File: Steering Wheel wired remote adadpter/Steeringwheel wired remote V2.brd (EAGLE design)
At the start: 100 x 80 mm, 8 parts

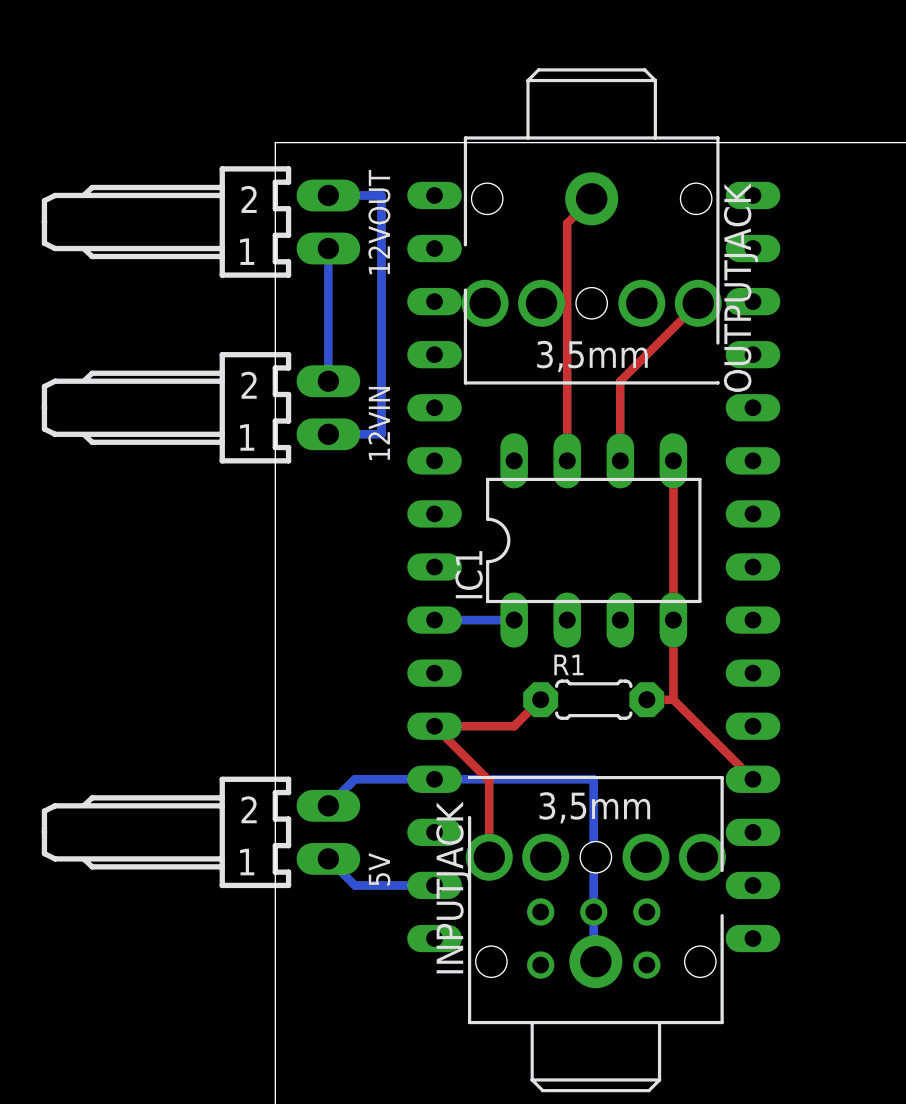
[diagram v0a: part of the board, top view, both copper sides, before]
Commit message: 3 pin jacks added
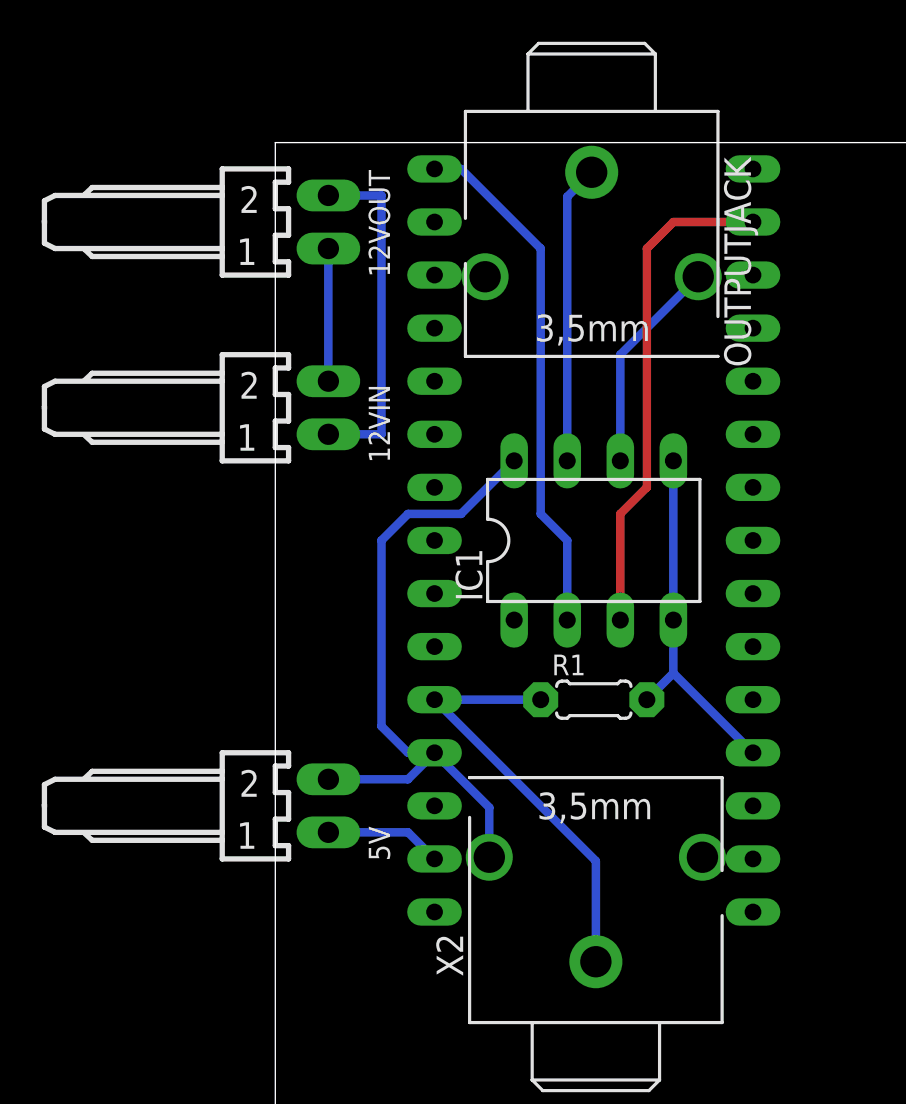
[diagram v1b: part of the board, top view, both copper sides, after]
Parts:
- removed INPUTJACK: STEREOJACK, adafruit:STX3100
- removed U$1: NANO, Arduino-clone:NANO
- added U$2: NANO, my_lib:NANO_NOISPC
- added X2: STEREOJACK_3PIN3PIN, my_lib:STX3000
- IC1: value (none) -> MCP4131
- OUTPUTJACK: value STEREOJACK -> STEREOJACK_3PIN3PIN; device adafruit:STX3100 -> my_lib:STX3000
- moved OUTPUTJACK 1.27 mm to (15.2, 78.7)
- moved 5V 1.27 mm to (2.54, 48.3)
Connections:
- removed net N$10: 5V.2, INPUTJACK.1, U$1.5V
- removed net N$11: IC1.1, U$1.A5
- new net N$2: IC1.2, U$2.D13
- net N$1: now also IC1.3, U$2.D11; no longer IC1.4, IC1.5, R1.2, U$1.GND1
- net N$3: now also IC1.4, IC1.5, R1.2, U$2.GND1; no longer IC1.2, U$1.D13
- net N$4: now also R1.1, U$2.A7, X2.1; no longer IC1.3, U$1.D11
- net N$6: now also 5V.2, IC1.8, U$2.5V, X2.2; no longer INPUTJACK.2, R1.1, U$1.A7
- net N$7: now also U$2.GND; no longer IC1.8, U$1.GND
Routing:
- net N$2: track 0.00 -> 25.0 mm
- net N$10: track 22.3 -> 0.00 mm, vias 1 -> 0
- net N$4: track 0.00 -> 20.8 mm
- net N$6: track 13.0 -> 31.6 mm
- net N$3: track 0.00 -> 17.3 mm
- net N$1: track 18.1 -> 23.9 mm
- net N$11: track 3.81 -> 0.00 mm
- net N$5: track 9.09 -> 10.4 mm
- net N$12: track 13.0 -> 14.3 mm

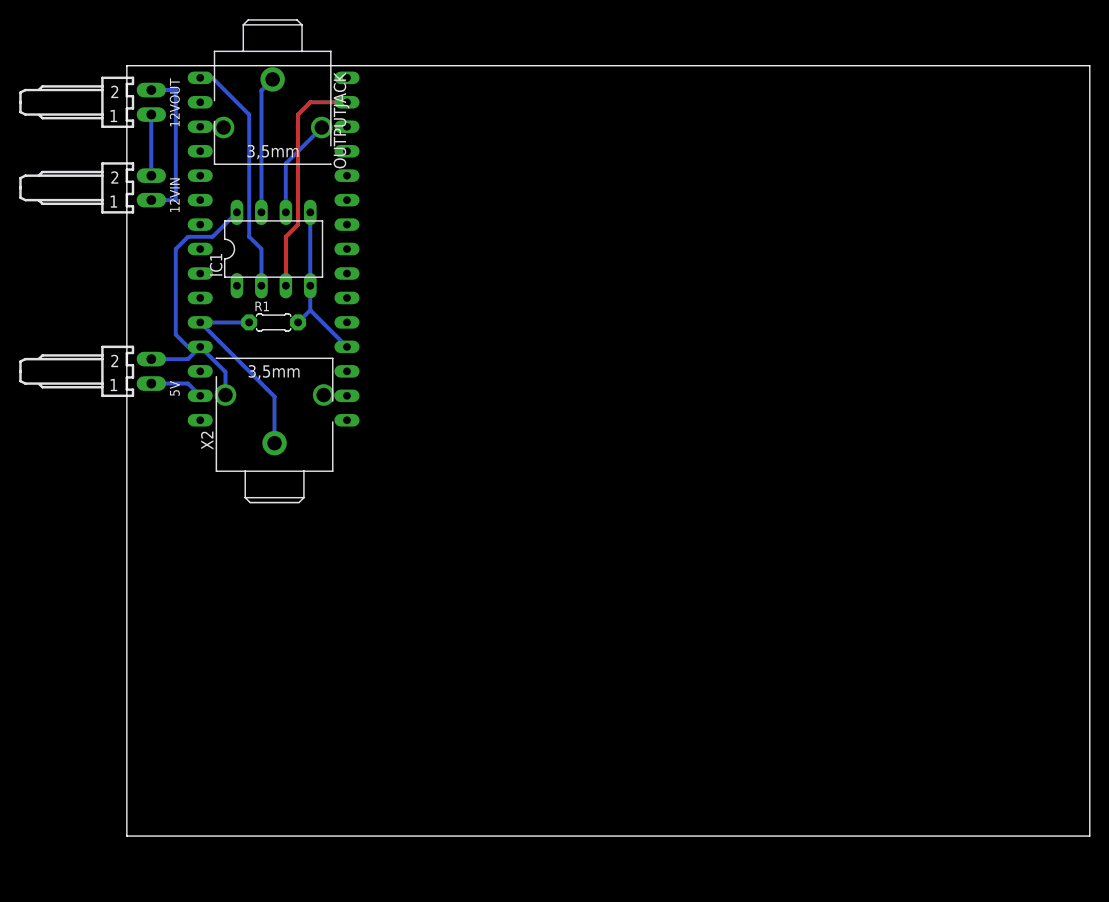
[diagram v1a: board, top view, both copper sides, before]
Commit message: GND copper poor and .024 traces
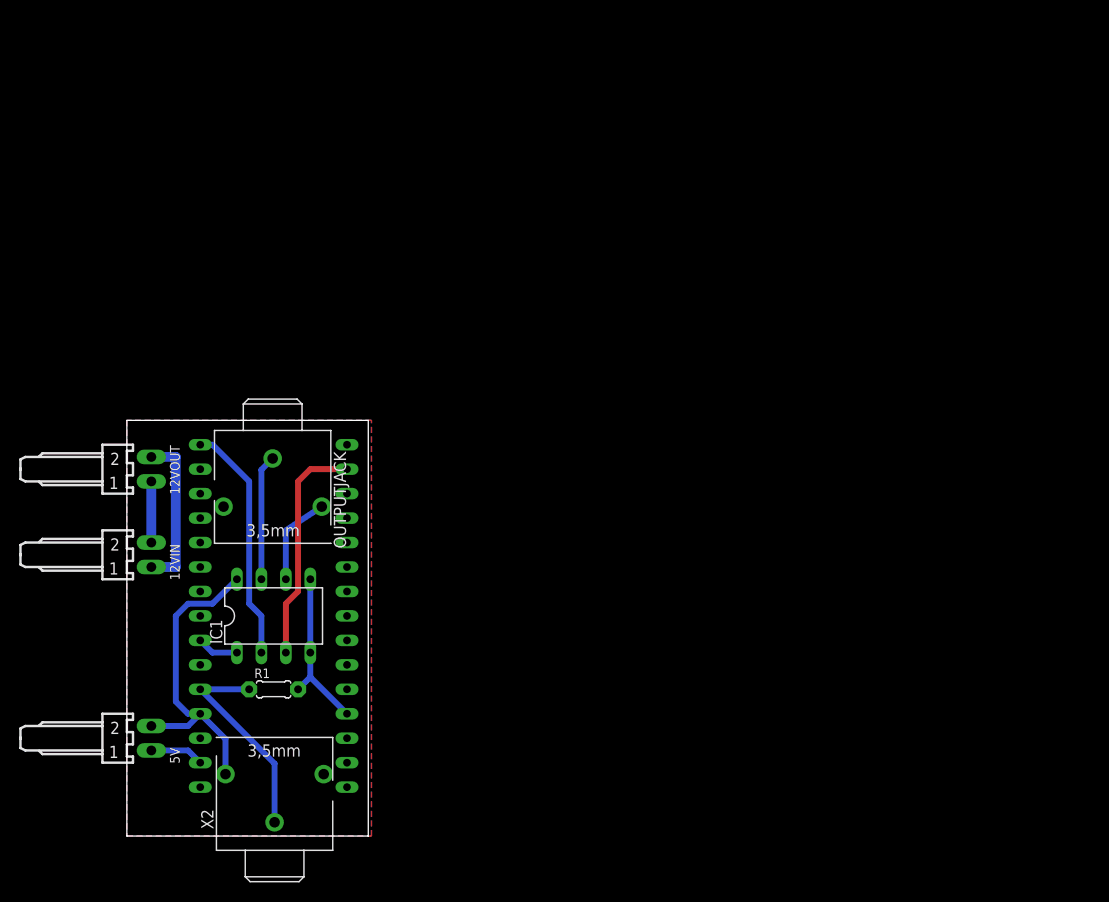
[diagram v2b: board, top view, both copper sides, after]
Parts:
- moved OUTPUTJACK 39.4 mm to (15.2, 39.4)
- moved X2 39.4 mm to (15.2, 1.27)
- moved 12VIN 38.1 mm to (2.54, 29.2)
- moved 12VOUT 38.1 mm to (2.54, 38.1)
- moved IC1 38.1 mm to (15.2, 22.9)
- moved R1 38.1 mm to (15.2, 15.2)
- moved U$2 38.1 mm to (17.8, 14.0)
- moved 5V 38.1 mm to (2.54, 10.2)
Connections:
- removed net N$3: IC1.4, IC1.5, R1.2, U$2.GND1
- removed net N$7: 5V.1, U$2.GND
- new net GND: 5V.1, IC1.4, IC1.5, R1.2, U$2.GND, U$2.GND1
- new net N$10: IC1.1, U$2.A5
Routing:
- net GND: track 0.00 -> 23.0 mm
- net N$3: track 17.3 -> 0.00 mm
- net N$7: track 5.61 -> 0.00 mm
- net N$10: track 0.00 -> 4.34 mm
- net N$6: track 31.6 -> 32.8 mm
- net N$12: track 14.3 -> 13.0 mm
- net N$4: track 20.8 -> 22.1 mm
- net N$5: track 10.4 -> 9.55 mm
- added copper zone on layer 1, net GND
- added copper zone on layer 16, net GND
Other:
- board size 100 x 80 mm -> 25.1 x 43.2 mm

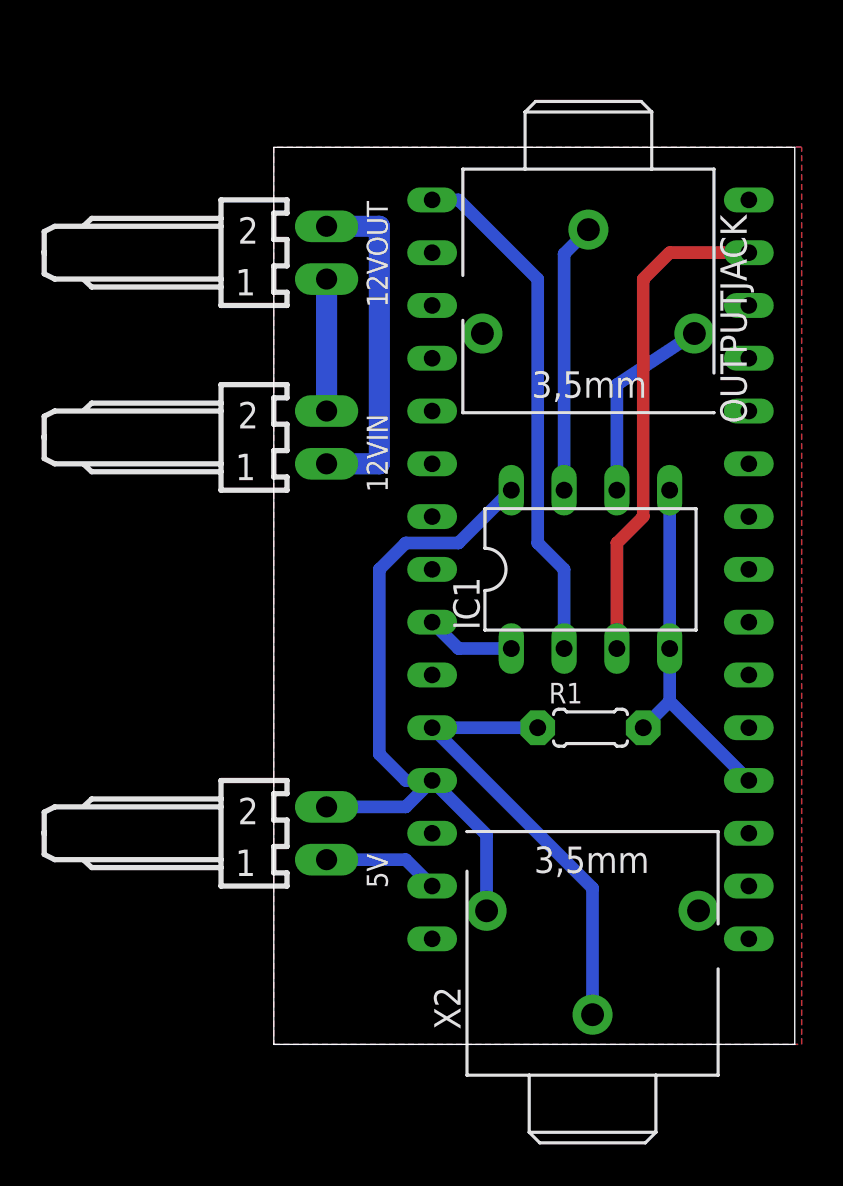
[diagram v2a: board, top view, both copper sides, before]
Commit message: mounting holes
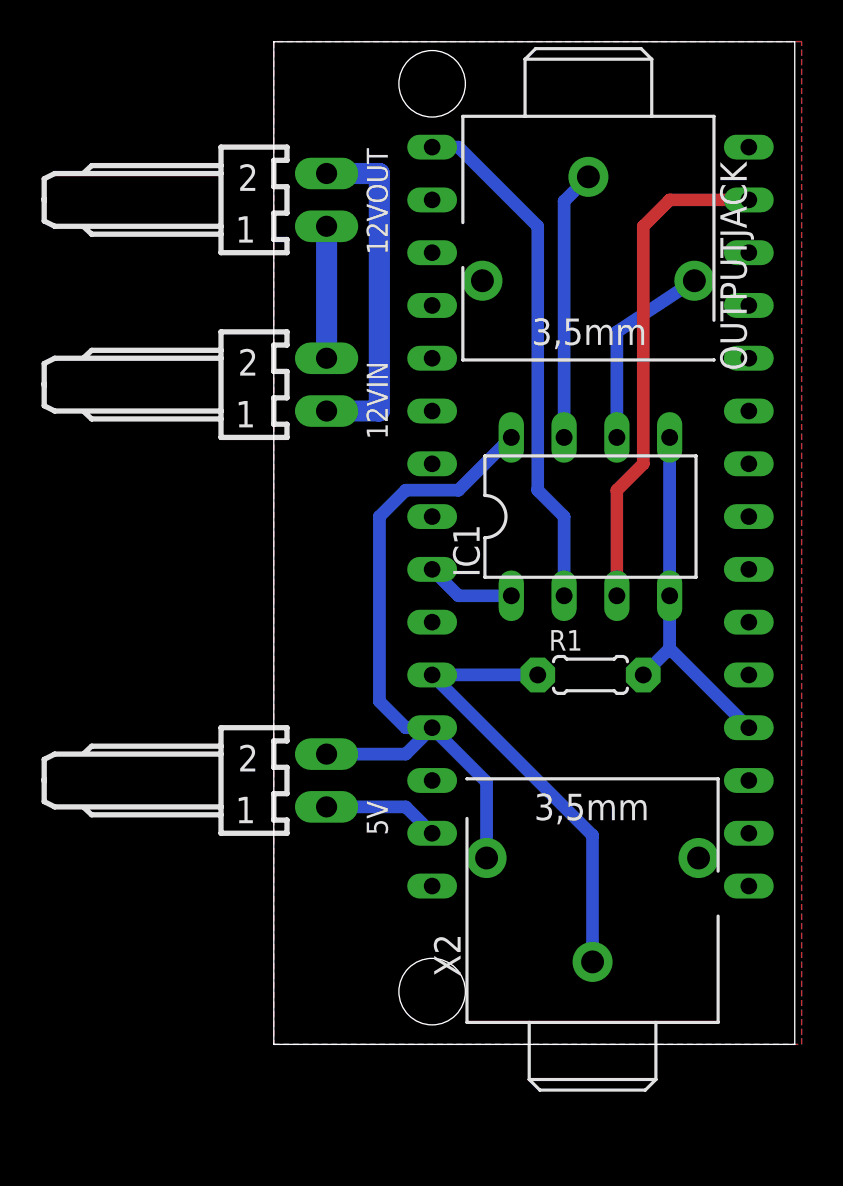
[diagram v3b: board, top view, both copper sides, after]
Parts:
- moved R1 2.54 mm to (15.2, 17.8)
- moved U$2 2.54 mm to (17.8, 16.5)
- moved X2 2.54 mm to (15.2, 3.81)
- moved 12VIN 2.54 mm to (2.54, 31.8)
- moved 12VOUT 2.54 mm to (2.54, 40.6)
- moved 5V 2.54 mm to (2.54, 12.7)
- moved IC1 2.54 mm to (15.2, 25.4)
- moved OUTPUTJACK 2.54 mm to (15.2, 41.9)
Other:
- board size 25.1 x 43.2 mm -> 25.1 x 48.2 mm
